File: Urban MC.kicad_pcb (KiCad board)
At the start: 4 copper layers, 166.4 x 125.1 mm, 78 parts, among them J1 Conn_01x02, J2 Conn_01x02, J3 Conn_01x03, J4 Conn_01x02, Q1 IQE022N06LM5CGSCATMA1, Q10 IQE022N06LM5CGSCATMA1, Q11 IQE022N06LM5CGSCATMA1, Q12 IQE022N06LM5CGSCATMA1, Q13 IQE022N06LM5CGSCATMA1, Q14 IQE022N06LM5CGSCATMA1, Q15 IQE022N06LM5CGSCATMA1, Q16 IQE022N06LM5CGSCATMA1, Q17 IQE022N06LM5CGSCATMA1, Q18 IQE022N06LM5CGSCATMA1, Q19 IQE022N06LM5CGSCATMA1, Q2 IQE022N06LM5CGSCATMA1, Q20 IQE022N06LM5CGSCATMA1, Q21 IQE022N06LM5CGSCATMA1, Q22 IQE022N06LM5CGSCATMA1, Q23 IQE022N06LM5CGSCATMA1, Q24 IQE022N06LM5CGSCATMA1, Q3 IQE022N06LM5CGSCATMA1, Q4 IQE022N06LM5CGSCATMA1, Q5 IQE022N06LM5CGSCATMA1, Q6 IQE022N06LM5CGSCATMA1, Q7 IQE022N06LM5CGSCATMA1, Q8 IQE022N06LM5CGSCATMA1, Q9 IQE022N06LM5CGSCATMA1, SW1 CAN_TERM, SW2 SW_Push, U1 MCP2561/2, U2 MCP4725, U3 MCP2515-xSO, Y1 8MHz

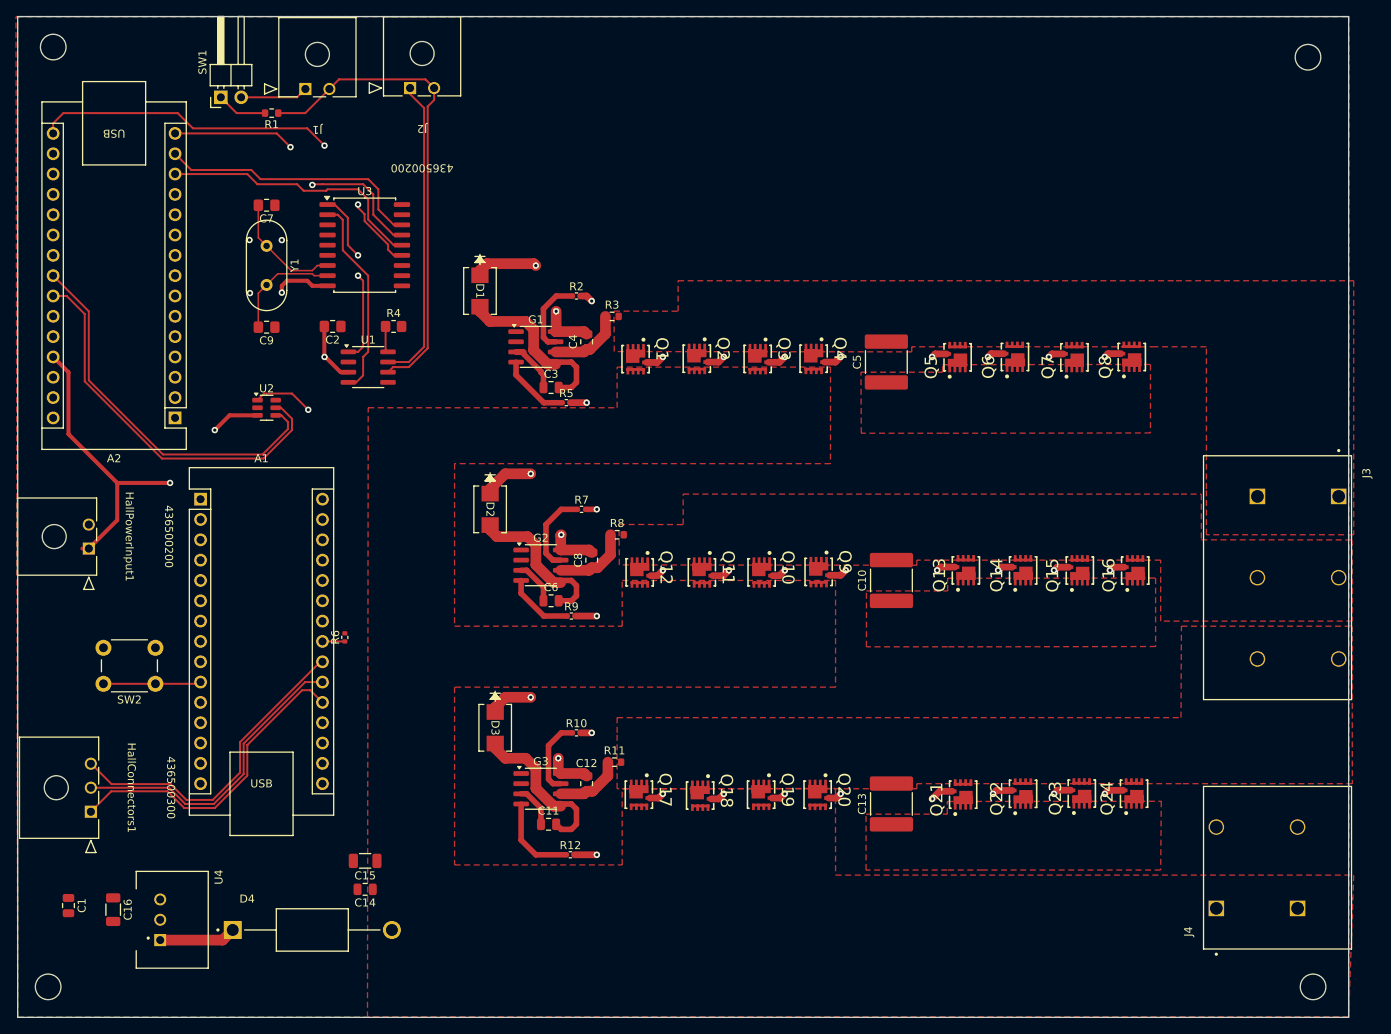
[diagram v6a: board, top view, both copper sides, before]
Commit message: in the middle of layout changes- expanding right side and drawing gate driver traces
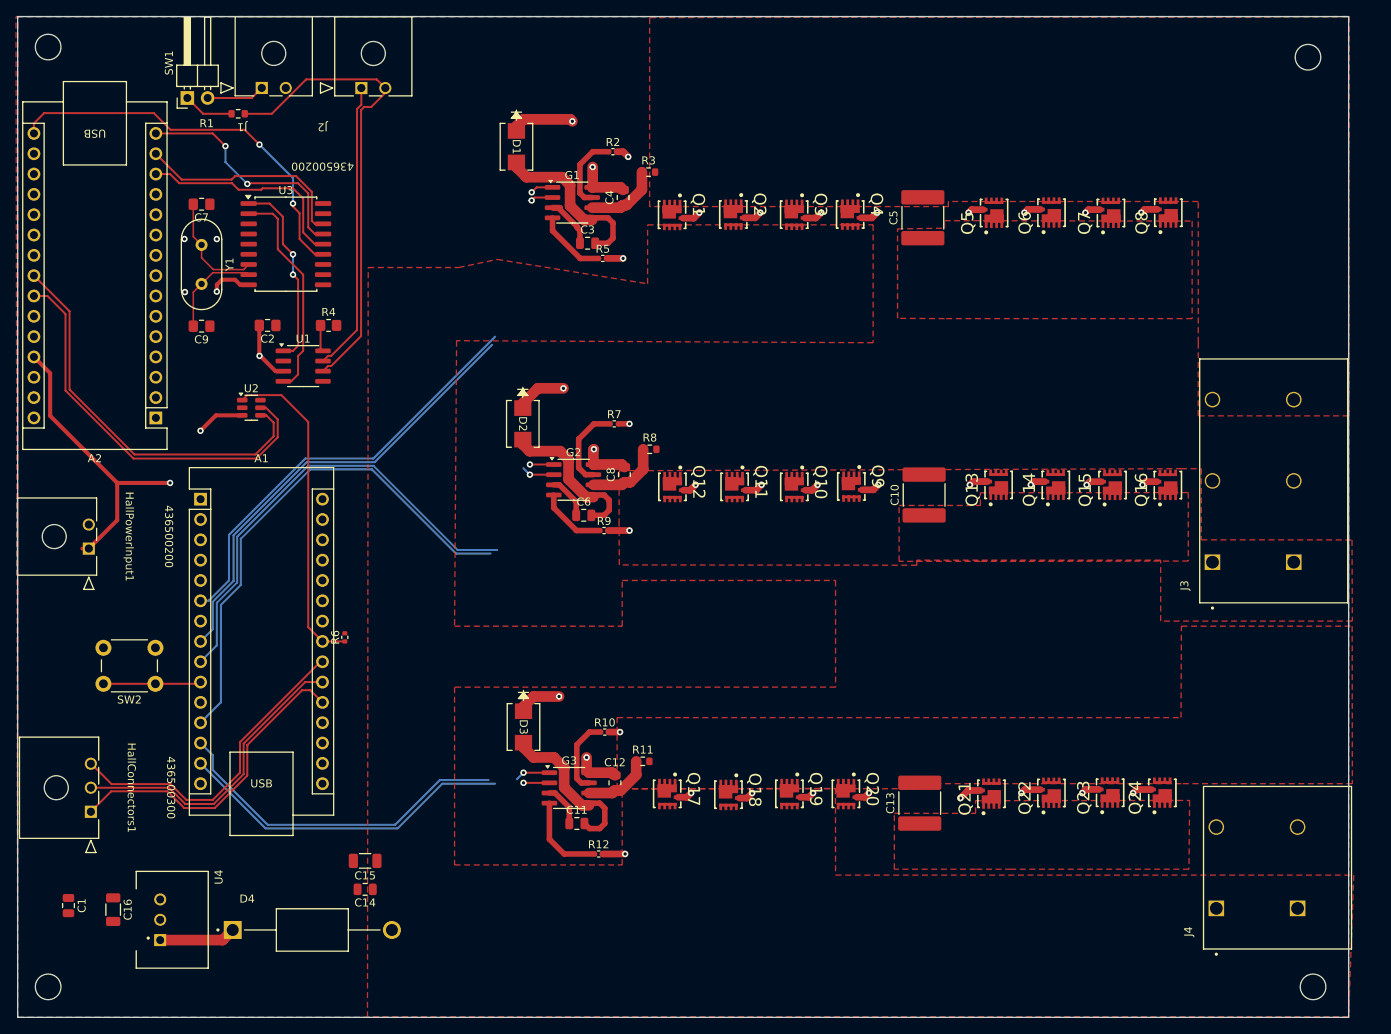
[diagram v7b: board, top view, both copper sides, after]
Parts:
- moved Q5 18.6 mm to (214.6, 53.1)
- moved Q7 18.6 mm to (229.2, 53.1)
- moved C3 18.6 mm to (163.9, 56.9)
- moved C5 18.6 mm to (205.9, 53.7)
- moved G1 18.6 mm to (162.0, 51.8)
- moved Q3 18.6 mm to (190.0, 53.3)
- moved Q4 18.6 mm to (197.0, 53.3)
- moved Q6 18.6 mm to (221.7, 53.1)
- moved R2 18.6 mm to (167.1, 45.5)
- moved R3 18.6 mm to (171.6, 48.0)
- moved D1 18.6 mm to (155.1, 44.8)
- moved Q1 18.6 mm to (174.7, 53.4)
- moved Q2 18.6 mm to (182.4, 53.3)
- moved Q8 18.6 mm to (236.3, 53.1)
- moved R5 18.6 mm to (165.9, 58.8)
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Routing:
- net Net-(A1-D9): track 0.00 -> 68.4 mm, vias 0 -> 1
- net Net-(A1-D6): track 0.00 -> 61.1 mm, vias 0 -> 1
- net Net-(A1-D5): track 0.00 -> 60.3 mm, vias 0 -> 1
- net Net-(A1-D3): track 0.00 -> 56.7 mm, vias 0 -> 1
- net Net-(A1-D10): track 0.00 -> 48.0 mm, vias 0 -> 1
- net Net-(A1-D11): track 0.00 -> 45.8 mm, vias 0 -> 1
- net SO: track 36.4 -> 29.8 mm
- net SI: track 33.5 -> 27.0 mm
- net SCK: track 55.7 -> 49.2 mm
- net CS: track 33.7 -> 27.2 mm
- net +5V: track 101.8 -> 96.0 mm
- net /CAN HIGH: track 38.4 -> 36.3 mm
- net /A5: track 48.7 -> 50.6 mm
- net /A4: track 47.7 -> 49.6 mm
- net Net-(U1-TXD): track 22.2 -> 24.0 mm
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- removed copper zone on F.Cu, net Net-(J3-Pin_1)

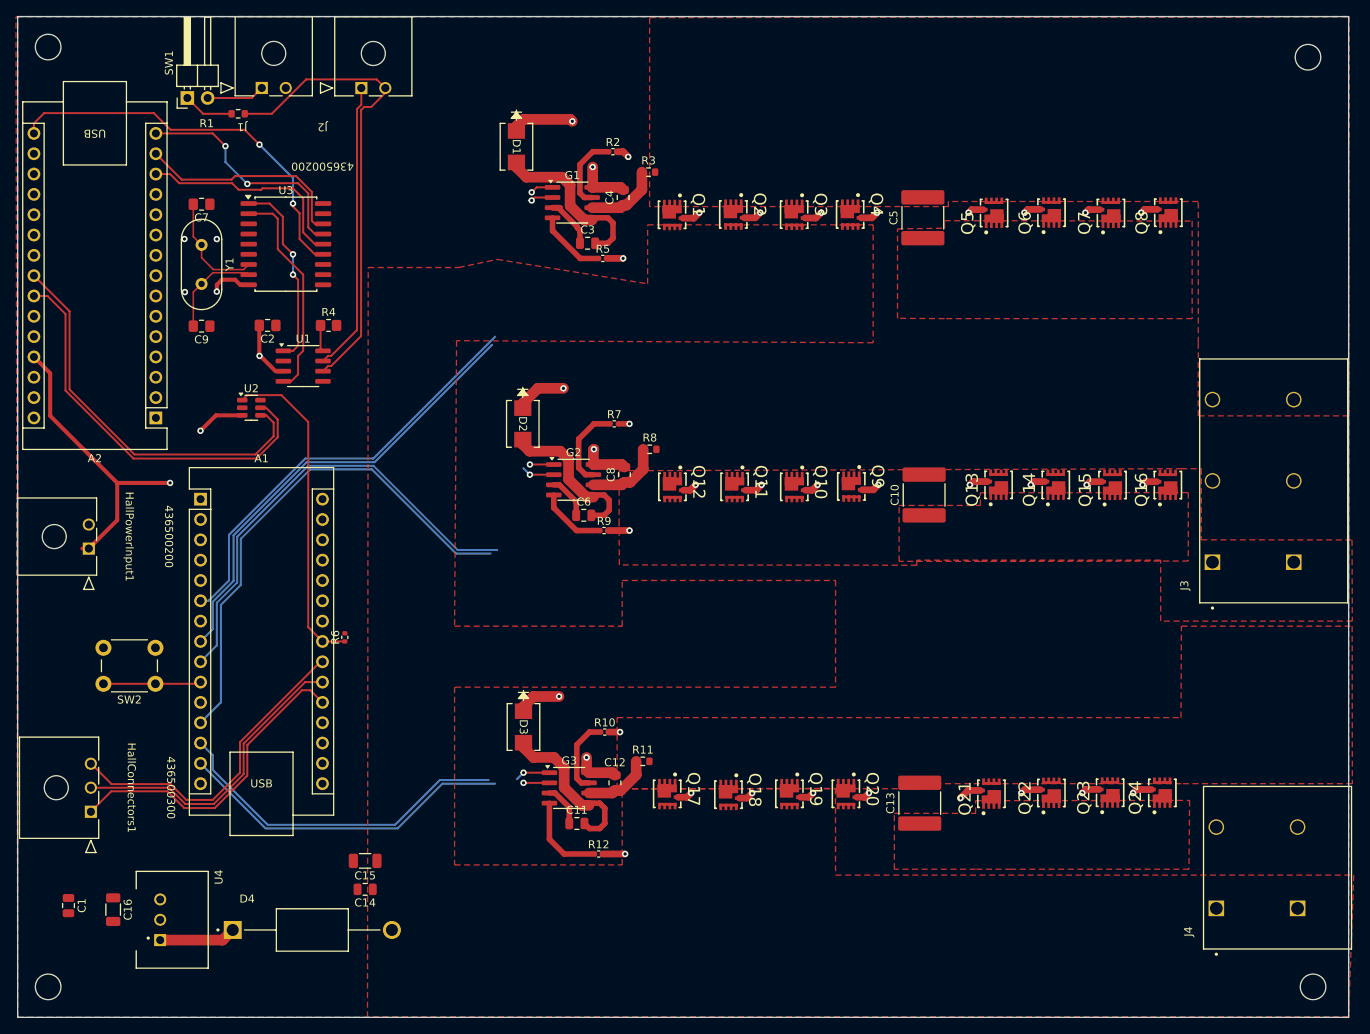
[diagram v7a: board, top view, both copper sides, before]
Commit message: filledempty space with filled zones, grounded components
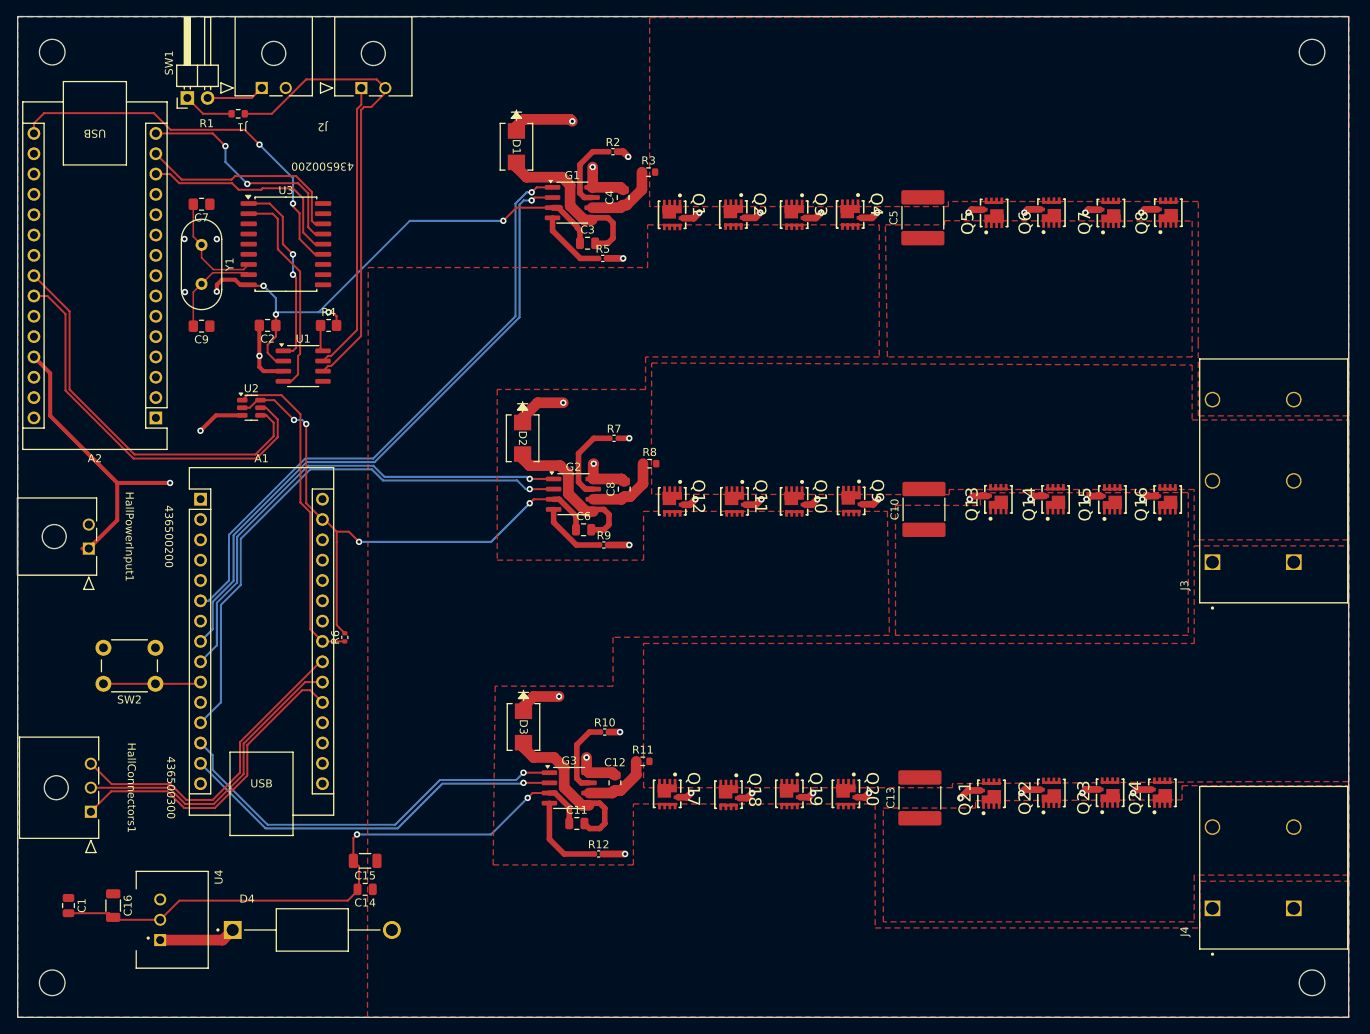
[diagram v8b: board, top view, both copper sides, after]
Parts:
- moved C10 1.80 mm to (206.0, 90.2)
- moved C8 1.80 mm to (168.5, 87.6)
- moved Q10 1.80 mm to (190.0, 89.2)
- moved Q11 1.80 mm to (182.5, 89.2)
- moved Q12 1.80 mm to (174.7, 89.2)
- moved Q15 1.80 mm to (229.3, 88.9)
- moved Q16 1.80 mm to (236.3, 88.9)
- moved R7 1.80 mm to (167.3, 81.3)
- moved C6 1.80 mm to (163.4, 92.7)
- moved D2 1.80 mm to (155.8, 81.3)
- moved G2 1.80 mm to (162.2, 88.3)
- moved Q13 1.80 mm to (215.1, 88.9)
- moved Q9 1.80 mm to (197.1, 89.1)
- moved R8 1.80 mm to (171.7, 84.5)
- moved R9 1.80 mm to (166.0, 94.6)
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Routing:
- net GND: track 23.2 -> 220.3 mm, vias 4 -> 14
- net Net-(A1-D5): track 60.3 -> 80.6 mm
- net Net-(A1-D3): track 56.7 -> 77.0 mm
- net Net-(A1-D11): track 45.8 -> 49.3 mm
- net Net-(A1-D10): track 48.0 -> 51.6 mm
- net +5V: track 96.0 -> 96.9 mm
- added copper zone on F.Cu, net Net-(J3-Pin_1)
